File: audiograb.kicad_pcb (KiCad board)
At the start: 4 copper layers, 167 x 69.7 mm, 135 parts, among them IC1 USB2244I-AEZG-06, J1 USB_C_Receptacle_USB2.0_16P, J10 20579-001E, J11 732511150, J12 732511150, J13 732511150, J14 732511150, J15 F32Q-1A7H1-11022, J16 MEM2075-00-140-01-A, J17 3V5_out, J2 SAM10346-ND, J3 SAM10346-ND, J4 JST-PH, J5 12V_in, J6 20579-001E, J7 20579-001E, J8 20579-001E, J9 M.2_Socket_B, M1 ComputeModule5-CM5, P1 SF72S006VBDR2500, Q1 Q_PMOS_GSD, Q2 DMT6007LFG-7, Q3 NX3008NBKW_115, SW1 1825910-6, U1 LMR51450SDRRR, U10 CD4043BDR, U11 TPS22919DCKR, U12 IP4220CZ6F, U2 LM74700QDBVTQ1, U3 LMR51450SDRRR, U8 MAX4996LETG_

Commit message: bytta ut TP-loops med pads, begynt modem-cm layout
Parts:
- TP1, TP2, TP3, TP4, TP5: footprint TestPoint:TestPoint_Loop_D2.60mm_Drill1.6mm_Beaded -> TestPoint:TestPoint_Pad_D1.0mm; moved to B.Cu
- moved TP1 117.6 mm to (142.1, 96.2), turned to 0 degrees
- moved TP2 111.3 mm to (141.6, 104.5), turned to 0 degrees
- moved TP4 109.0 mm to (144.2, 107.6), turned to 0 degrees
- moved C5 106.5 mm to (144.1, 94.0)
- moved D1 106.5 mm to (144.1, 96.1)
- moved P1 106.5 mm to (144.2, 104.2)
- moved R20 106.5 mm to (138.1, 101.5)
- moved TP3 106.1 mm to (141.7, 107.6), turned to 0 degrees
- moved TP5 102.3 mm to (146.6, 107.7), turned to 0 degrees
- moved CR3 92.0 mm to (149.8, 94.1)
- moved J13 65.2 mm to (191.6, 82.3)
- moved J8 65.2 mm to (185.5, 82.3)
- moved J14 64.2 mm to (191.6, 53.9)
- moved J10 64.2 mm to (185.5, 53.7)
- moved C43 61.5 mm to (163.3, 109.5), turned to 0 degrees
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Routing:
- net /modem/USIM1_VDD: track 51.0 -> 18.3 mm
- net Net-(P1-I/O): track 30.4 -> 9.75 mm
- net Net-(P1-CLK): track 29.4 -> 10.1 mm
- net Net-(P1-RST): track 28.5 -> 13.9 mm
- net /BMS-TX: track 56.8 -> 60.6 mm
- net /BMS-RX: track 56.3 -> 59.9 mm
- net +3V3_CM5: track 362.9 -> 365.3 mm
- net /modem/USIM1_DET: track 2.67 -> 4.07 mm, vias 0 -> 1
- net Net-(CR3-Pad5): track 0.00 -> 0.89 mm
- net /USB2_P: track 36.1 -> 35.3 mm
- net /USB2_N: track 35.5 -> 34.8 mm
- net GND: vias 237 -> 235
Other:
- board size 167 x 69.7 mm -> 171 x 72 mm

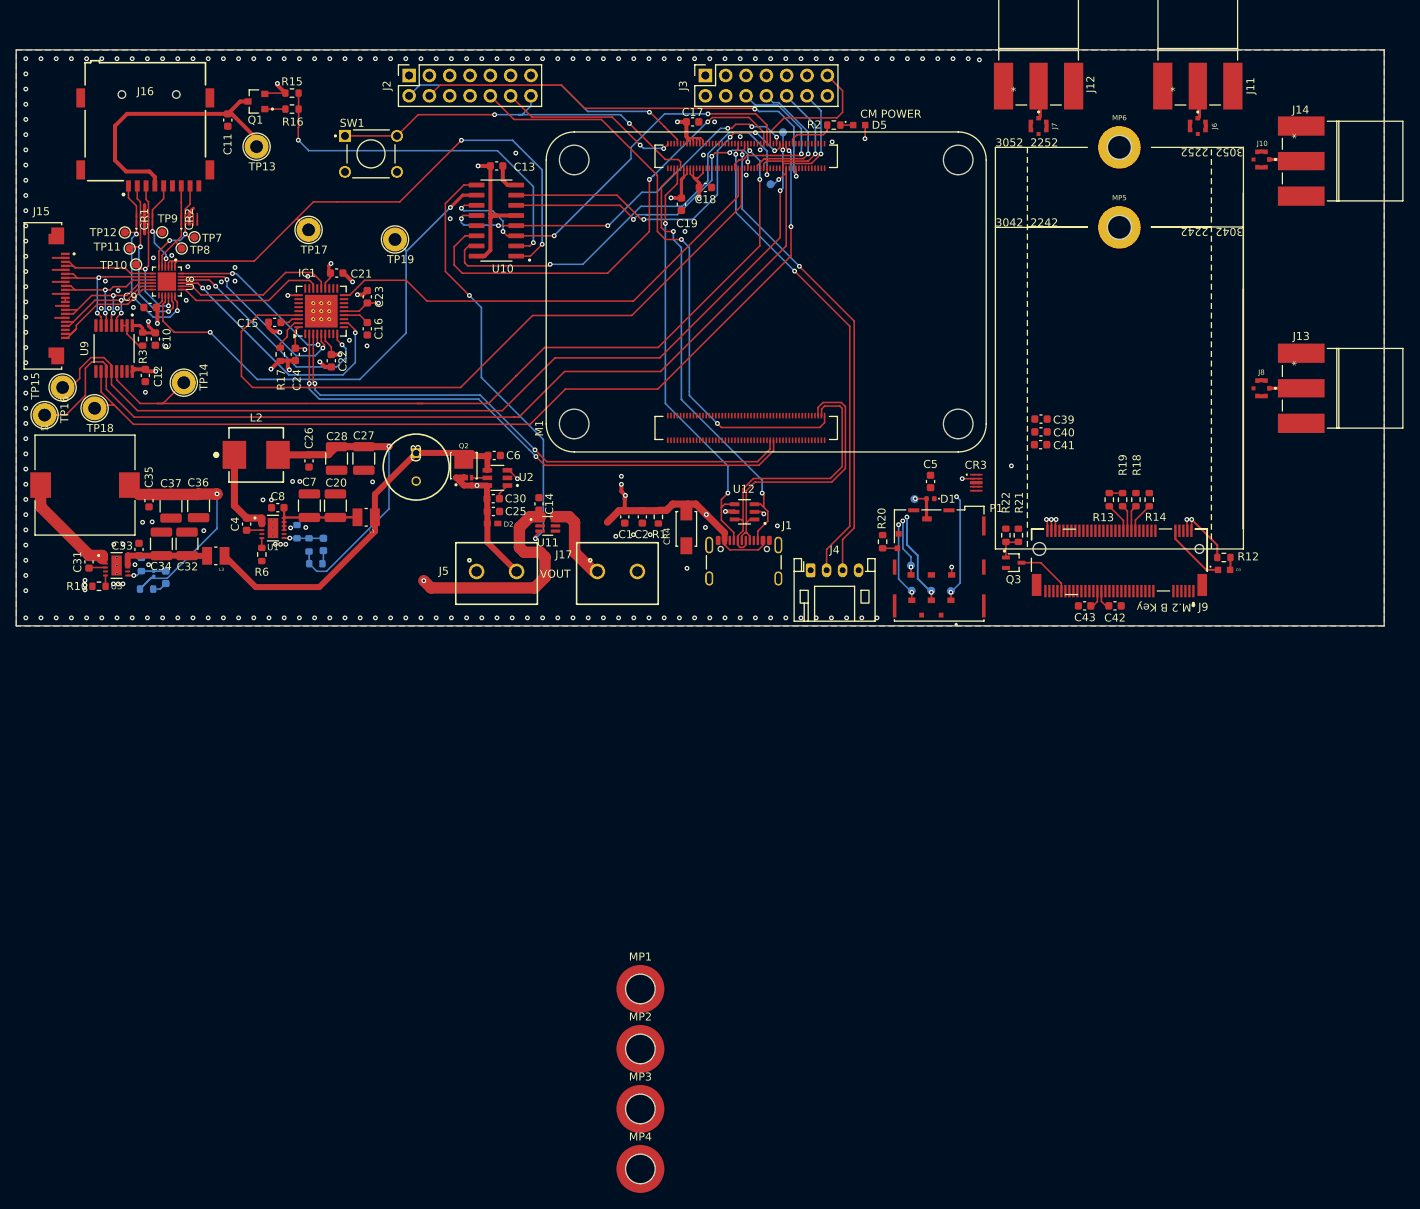
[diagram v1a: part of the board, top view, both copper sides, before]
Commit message: Fiksa all routing CM-Modem-SIM-GPIO++, mangle fill og rule zones
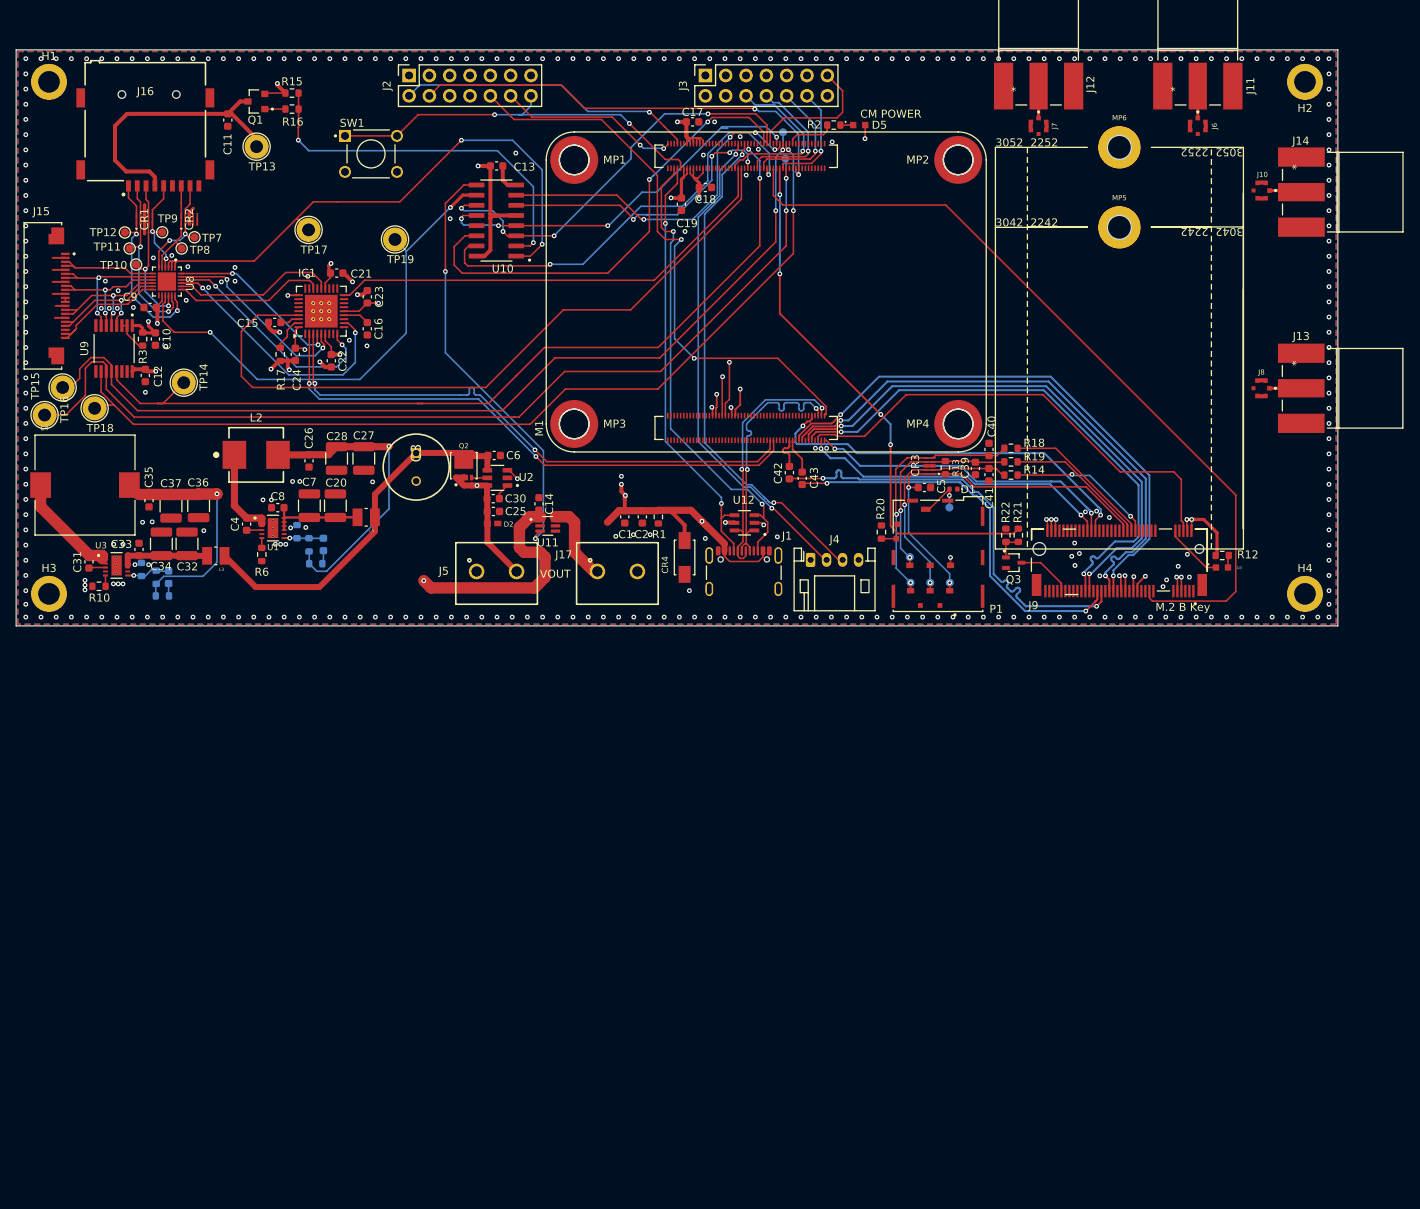
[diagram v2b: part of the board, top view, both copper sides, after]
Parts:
- added H1: MountingHole, MountingHole:MountingHole_2.7mm_M2.5_ISO14580_Pad, F.Cu at (33.9, 44.0)
- added H2: MountingHole, MountingHole:MountingHole_2.7mm_M2.5_ISO14580_Pad, F.Cu at (190.9, 44.0)
- added H3: MountingHole, MountingHole:MountingHole_2.7mm_M2.5_ISO14580_Pad, F.Cu at (33.9, 108.0)
- added H4: MountingHole, MountingHole:MountingHole_2.7mm_M2.5_ISO14580_Pad, F.Cu at (190.9, 108.0)
- R8: footprint Resistor_SMD:R_0201_0603Metric -> Resistor_SMD:R_0603_1608Metric
- moved MP2 118.0 mm to (147.6, 53.8)
- moved MP1 104.0 mm to (99.5, 53.8)
- moved MP4 101.2 mm to (147.6, 86.8)
- moved MP3 86.0 mm to (99.5, 86.8)
- moved C42 44.0 mm to (126.5, 92.8), turned to -90 degrees
- moved C43 38.7 mm to (128.1, 93.5), turned to -90 degrees
- moved R13 20.9 mm to (145.9, 92.2)
- moved R14 17.6 mm to (154.2, 93.2), turned to 180 degrees
- moved R18 16.9 mm to (154.2, 89.8), turned to 180 degrees
- moved R19 14.7 mm to (154.2, 91.5), turned to 180 degrees
- moved C39 10.3 mm to (149.7, 92.3), turned to -90 degrees
- moved C41 7.46 mm to (151.4, 93.1), turned to -90 degrees
- moved C40 6.86 mm to (151.4, 90.0), turned to 90 degrees
- moved CR3 6.21 mm to (144.0, 92.0), turned to 180 degrees
- moved TP1 4.49 mm to (146.4, 97.2)
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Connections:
- net Net-(J9-PCIE_RX_M) renamed /modem/PCIE_RX_MOD_N
- net Net-(J9-PCIE_RX_P) renamed /modem/PCIE_RX_MOD_P
- CR3 pad 5: Net-(CR3-Pad5) -> Net-(P1-CLK)
- CR3 pad 6: Net-(CR3-Pad5) -> Net-(P1-CLK)
- J3 pad 4: +3V3_CM5 -> +5V
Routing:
- net /CM_WAKE_ON_WWAN: track 0.00 -> 101.1 mm
- net /USB3-1-D_N: track 0.00 -> 88.0 mm, vias 0 -> 2
- net /USB3-1-D_P: track 0.00 -> 87.8 mm, vias 0 -> 2
- net /USB3-1-TX_N: track 0.00 -> 84.2 mm, vias 0 -> 2
- net /USB3-1-TX_P: track 0.00 -> 84.2 mm, vias 0 -> 2
- net /USB3-1-RX_N: track 0.00 -> 79.8 mm, vias 0 -> 2
- net /USB3-1-RX_P: track 0.00 -> 79.6 mm, vias 0 -> 2
- net /PCIE_RX_N: track 0.00 -> 69.4 mm, vias 0 -> 2
- net /PCIE_RX_P: track 0.00 -> 69.3 mm, vias 0 -> 2
- net /PCIE_CLK_N: track 0.00 -> 67.4 mm, vias 0 -> 2
- net /PCIE_CLK_P: track 0.00 -> 67.4 mm, vias 0 -> 2
- net /MODEM_RESET_N: track 0.00 -> 67.2 mm, vias 0 -> 4
- net /PCIE_PWR_EN: track 0.00 -> 59.1 mm
- net /modem/PCIE_RX_MOD_N: track 2.11 -> 55.9 mm, vias 0 -> 2
- net /PCIE_nRST: track 0.00 -> 48.9 mm, vias 0 -> 2
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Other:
- board size 171 x 72 mm -> 165.2 x 72 mm
- board text added: "${REFERENCE}"

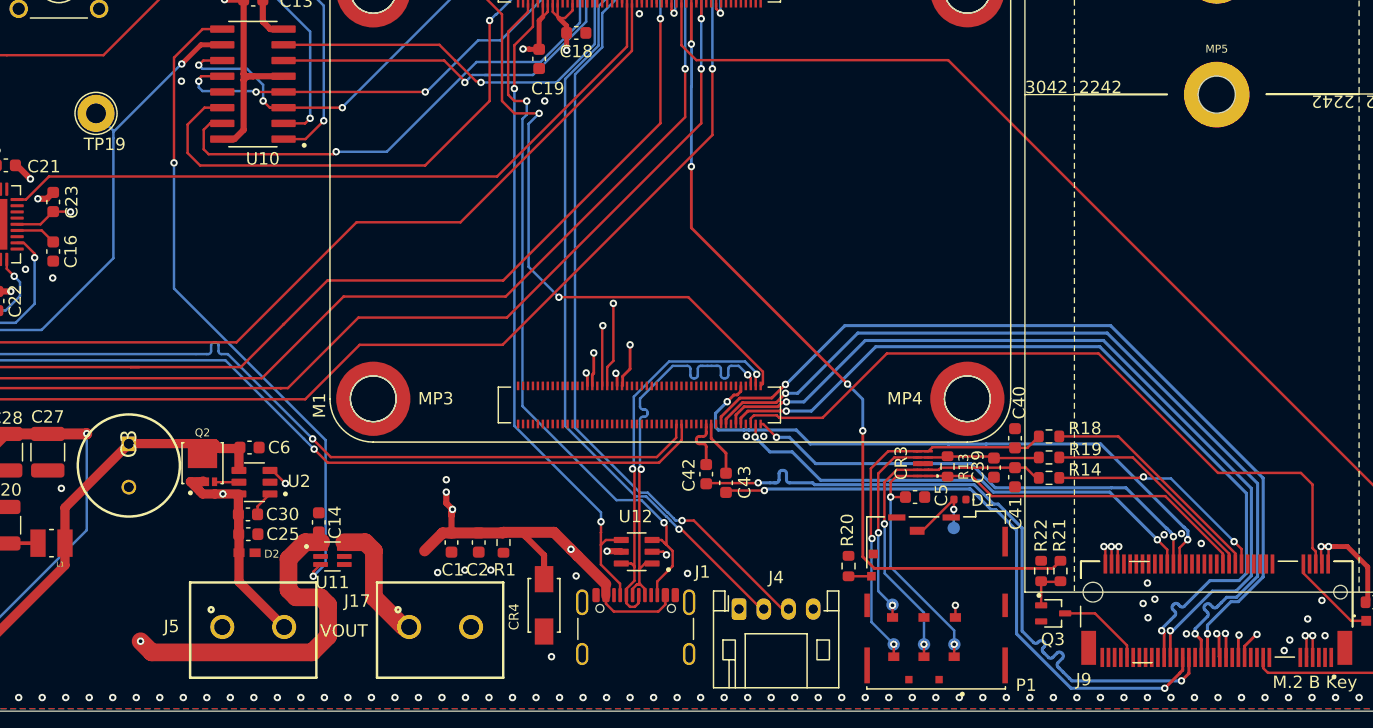
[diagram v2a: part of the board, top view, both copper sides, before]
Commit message: endret tykkelse layers, se over impedans til pwr på nytt! Mangler å legge til GND og keep-out zones osv, + litt småpuss
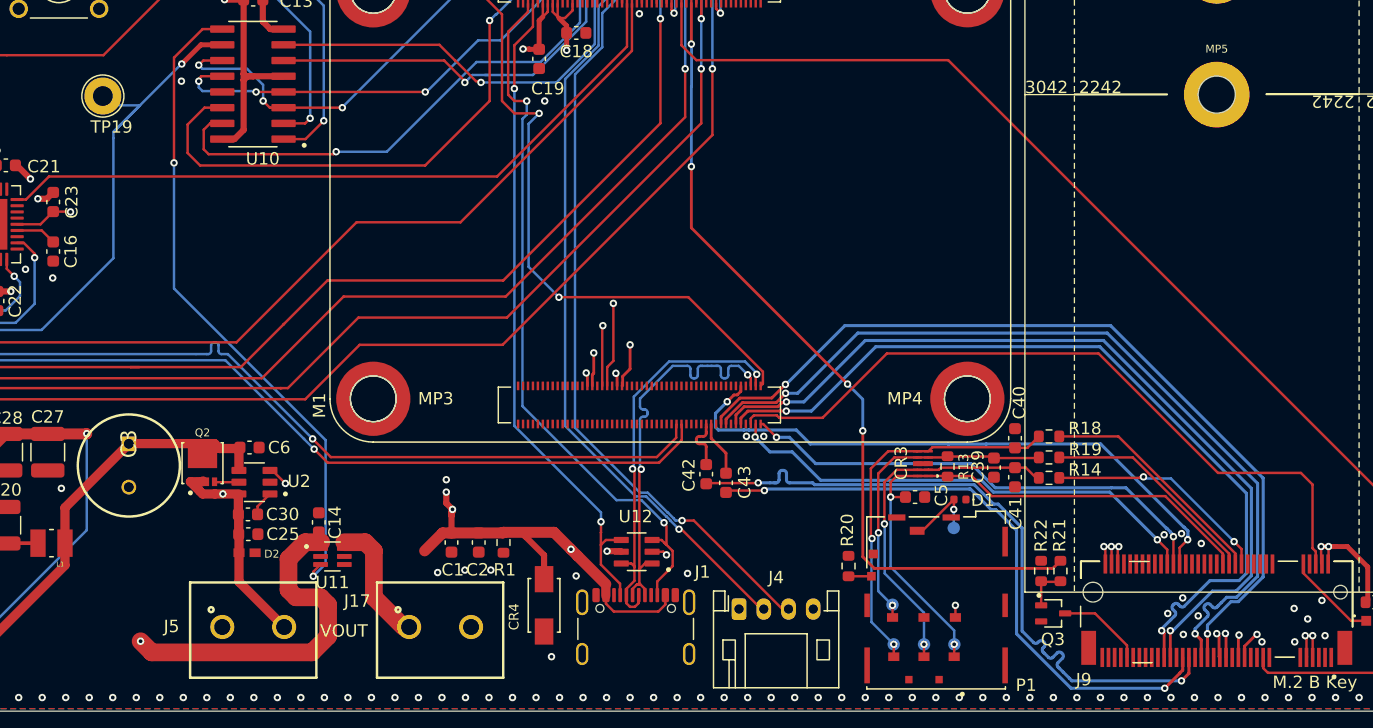
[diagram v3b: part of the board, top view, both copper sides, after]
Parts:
- moved TP19 1.50 mm to (77.7, 62.3)
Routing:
- net Net-(U10-Q3): track 63.2 -> 67.7 mm
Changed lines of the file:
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@@
 	(footprint "TestPoint:TestPoint_Loop_D2.60mm_Drill1.6mm_Beaded"
 		(layer "F.Cu")
-		(at 77.15 63.700001)
+		(at 77.7 62.3)
 		(descr "wire loop with bead as test point, loop diameter2.6mm, hole diameter 1.6mm")
 		(tags "test point wire loop bead")
@@
 	)
 	(via
-		(at 162.7 102.95)
+		(at 164.95 102.85)
 		(size 0.6)
 		(drill 0.3)
@@
 	)
 	(via
-		(at 165.25 105.75)
+		(at 165 105.8)
 		(size 0.6)
 		(drill 0.3)
@@
 	)
 	(via
-		(at 162.1 101.65)
+		(at 173.95 103.7)
 		(size 0.6)
 		(drill 0.3)
@@
 	)
 	(via
-		(at 173.15 107.1)
+		(at 171.35 106.4)
 		(size 0.6)
 		(drill 0.3)
@@
 	)
 	(via
-		(at 162.15 104.45)
+		(at 166.2 104.3)
 		(size 0.6)
 		(drill 0.3)
@@
 	)
 	(via
-		(at 161.75 103.3)
+		(at 163.740613 104.106791)
 		(size 0.6)
 		(drill 0.3)
@@
 	)
 	(via
-		(at 173.6 106.25)
+		(at 174 106.4)
 		(size 0.6)
 		(drill 0.3)
@@
 	)
 	(segment
+		(start 80.700001 63.05)
+		(end 77.15 63.05)
+		(width 0.2)
+		(layer "B.Cu")
+		(net 73)
+	)
+	(segment
 		(start 78.55 75.400001)
 		(end 72.75 81.200001)
@@
 	(segment
 		(start 78.55 65.200001)
-		(end 78.55 65.100001)
+		(end 80.700001 63.05)
 		(width 0.2)
 		(layer "B.Cu")
@@
 		(width 0.2)
 		(layer "B.Cu")
-		(net 73)
-	)
-	(segment
-		(start 78.55 65.100001)
-		(end 77.15 63.700001)
-		(width 0.2)
-		(layer "B.Cu")

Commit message: Homestretch
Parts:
- added G***: LOGO, LOGO, F.Cu at (172.8, 58.6)
- added G***: LOGO, LOGO, F.Cu at (147.3, 80.3)
- added G***: LOGO, LOGO, F.Cu at (101.9, 95.0)
- added G***: LOGO, LOGO, B.Cu at (138.6, 66.6)
- moved C27 0.75 mm to (72.5, 91.2)
- moved C28 0.75 mm to (69.1, 91.2)
- moved C26 0.70 mm to (65.7, 91.4)
- moved C3 0.30 mm to (79.5, 90.4)
- moved TP9 0.20 mm to (48.2, 62.8)
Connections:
- U1 pad 14: (no net) -> GND
- U1 pad 15: (no net) -> GND
- U1 pad 16: (no net) -> GND
- U3 pad 14: (no net) -> GND
- U3 pad 15: (no net) -> GND
- U3 pad 16: (no net) -> GND
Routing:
- net +3V5: track 108.3 -> 245.6 mm, vias 7 -> 15
- net GND: track 36.1 -> 92.8 mm, vias 340 -> 407
- net /modem/USIM1_DET: track 6.48 -> 23.3 mm
- net +3V3_CM5: track 369.4 -> 359.9 mm
- net +5V: track 172.5 -> 175.1 mm, vias 7 -> 12
- net /compute-module/USB_OTG_ID: track 71.8 -> 70.0 mm
- net /CM_WAKE_ON_WWAN: track 101.1 -> 102.7 mm, vias 0 -> 2
- net /PCIE_CLK_P: track 67.4 -> 66.7 mm
- net /CC2: track 57.6 -> 58.2 mm
- net Net-(J16-DAT0): track 12.5 -> 13.1 mm
- net /MODEM_RESET_N: track 67.2 -> 67.5 mm, vias 4 -> 2
- net /PCIE_PWR_EN: track 59.1 -> 59.2 mm, vias 0 -> 2
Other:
- outline, holes or cut-outs redrawn
- board text added: "AUDIOGRAB PCB V2.0 Åse B Opgård Sevat Skurtveit Jonas Hartberg Ove Ljosland"
- board text removed: "${REFERENCE}"
